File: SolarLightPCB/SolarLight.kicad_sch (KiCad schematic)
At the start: 17 parts, among them J1 I2C, J2 SPI, U1 TP4056, U2 WeMos_D1_mini, U3 MCP1700-3302E

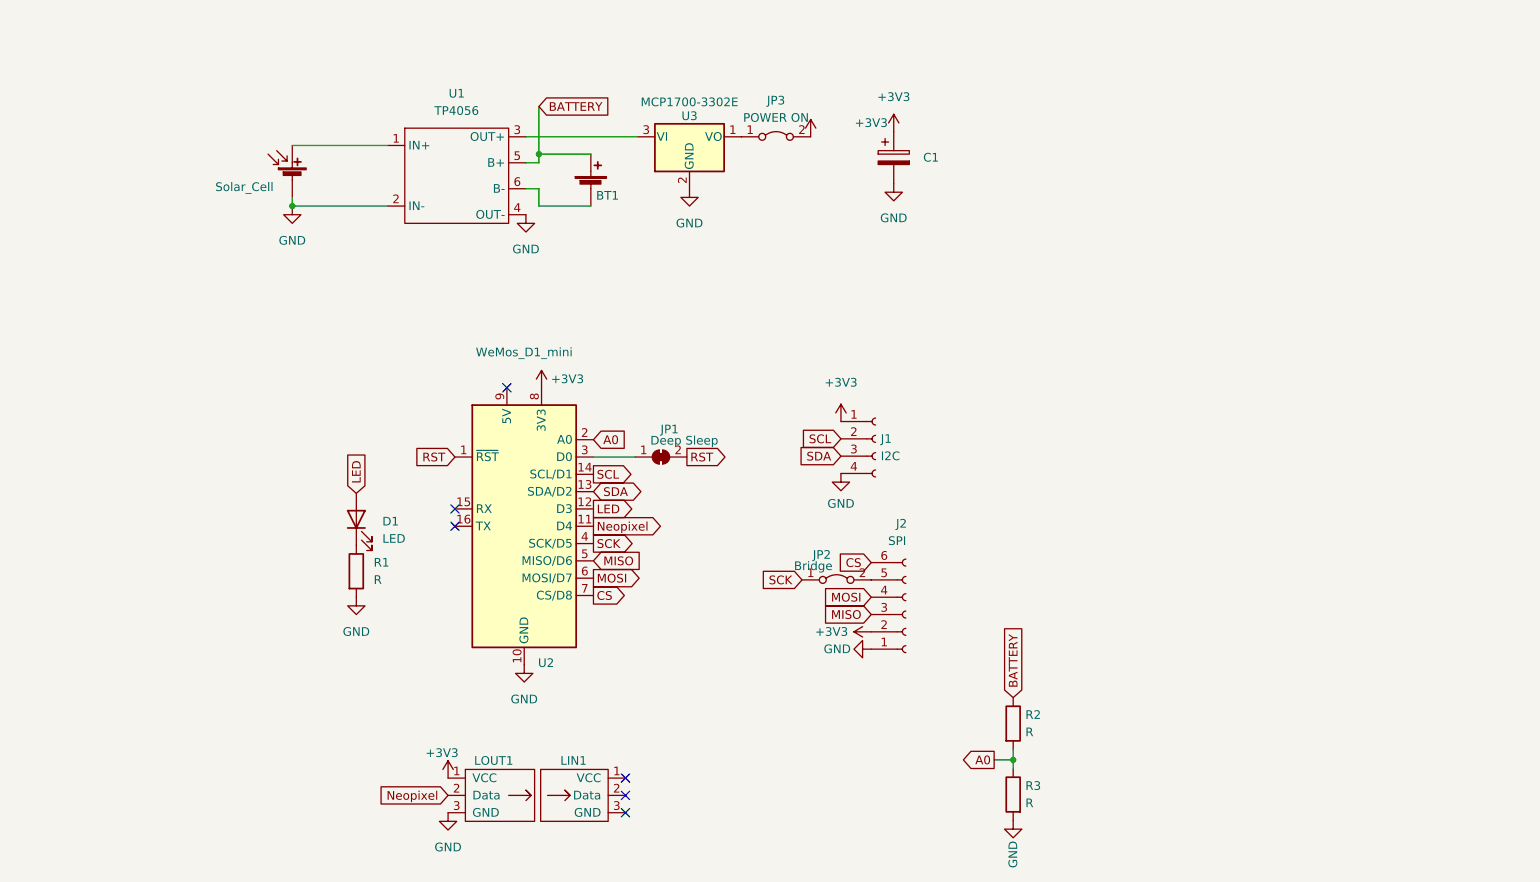
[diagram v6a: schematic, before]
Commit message: Add the output of the neopixel pin to GND
For now not the 3.3V since it’s hard to route that one over there
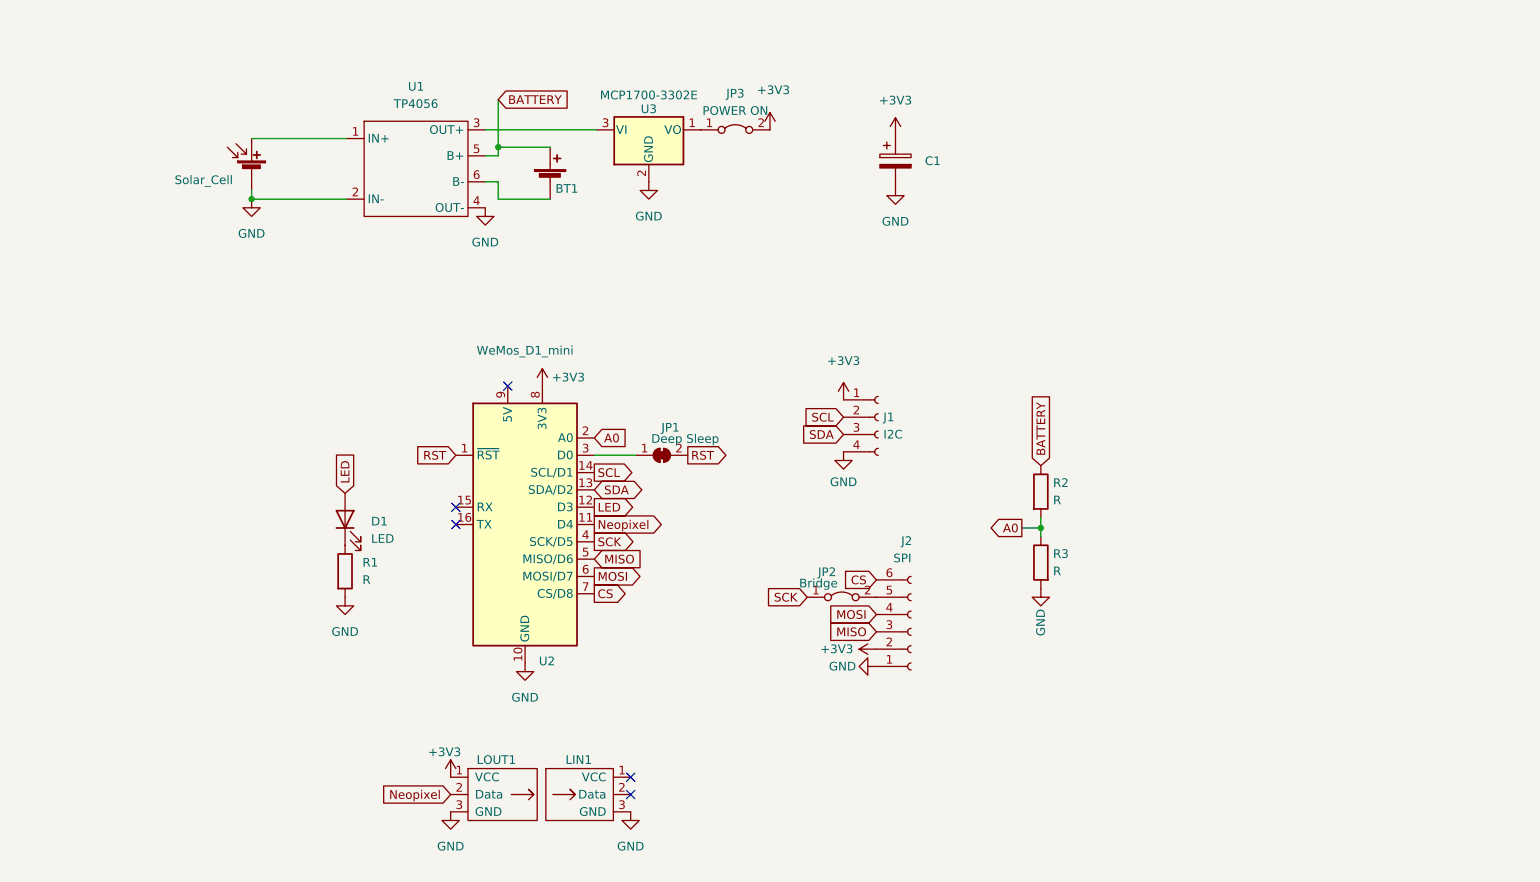
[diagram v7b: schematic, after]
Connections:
- net GND: now also LIN1.3 (GND)
- no-connect marks 6 -> 5
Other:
- moved on the sheet: BT1, C1, D1, J1, J2, JP2, JP3, LIN1, R1, R2, R3, U1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

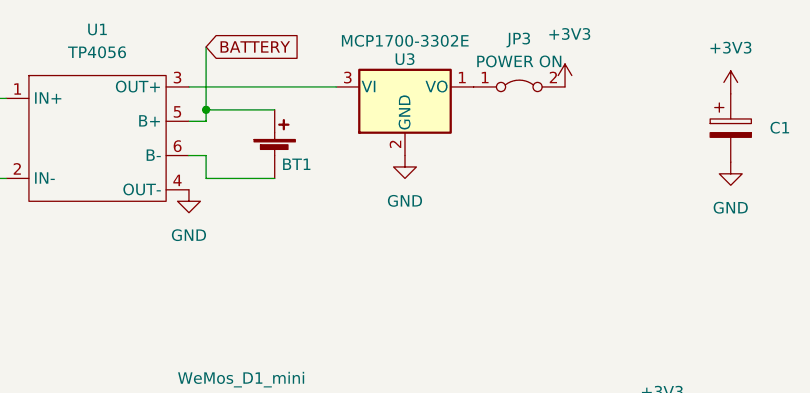
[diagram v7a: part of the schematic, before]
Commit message: Fix wrong pin numbering on the 3.3 voltage regulator
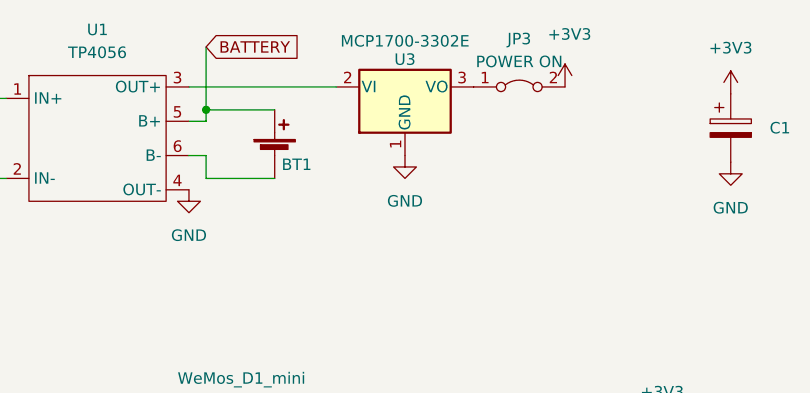
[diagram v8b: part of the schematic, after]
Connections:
- net GND: now also U3.1 (GND); no longer U3.2 (GND)
- net at JP3.1 (A): now also U3.3 (VO); no longer U3.1 (VO)
- net at U1.3 (OUT+): now also U3.2 (VI); no longer U3.3 (VI)
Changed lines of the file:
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@@
       (effects (font (size 1.27 1.27)) hide)
     )
-    (pin "1")
-    (pin "2")
-    (pin "3")
+    (pin "3")
+    (pin "1")
+    (pin "2")
   )
   (symbol (lib_id "power:GND") (at 185.42 85.852 0) (unit 1)
@@
   (symbol (lib_id "power:GND") (at 154.178 138.684 0) (unit 1)
     (in_bom yes) (on_board yes) (fields_autoplaced)
-    (property "Reference" "#PWR?" (id 0) (at 154.178 145.034 0)
+    (property "Reference" "#PWR0117" (id 0) (at 154.178 145.034 0)
       (effects (font (size 1.27 1.27)) hide)
     )
@@
     )
     (path "/c0094c7e-4def-4ceb-b93e-d1b073861880"
-      (reference "#PWR?") (unit 1) (value "GND") (footprint "")
+      (reference "#PWR0117") (unit 1) (value "GND") (footprint "")
     )
     (path "/1b639698-fdc2-412d-93eb-4fc53c894eea"
